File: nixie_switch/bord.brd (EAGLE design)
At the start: 20 x 25 mm, 2 parts, among them SW1 TVGP01-G73BB

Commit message: [fix] hole
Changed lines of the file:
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@@
 <wire x1="20" y1="25" x2="0" y2="25" width="0" layer="20"/>
 <wire x1="0" y1="25" x2="0" y2="0" width="0" layer="20"/>
-<hole x="2" y="23" drill="3.2"/>
-<hole x="18" y="23" drill="3.2"/>
-<hole x="18" y="2" drill="3.2"/>
-<hole x="2" y="2" drill="3.2"/>
+<hole x="17" y="6" drill="3.2"/>
+<hole x="3" y="6" drill="3.2"/>
 </plain>
 <attributes>

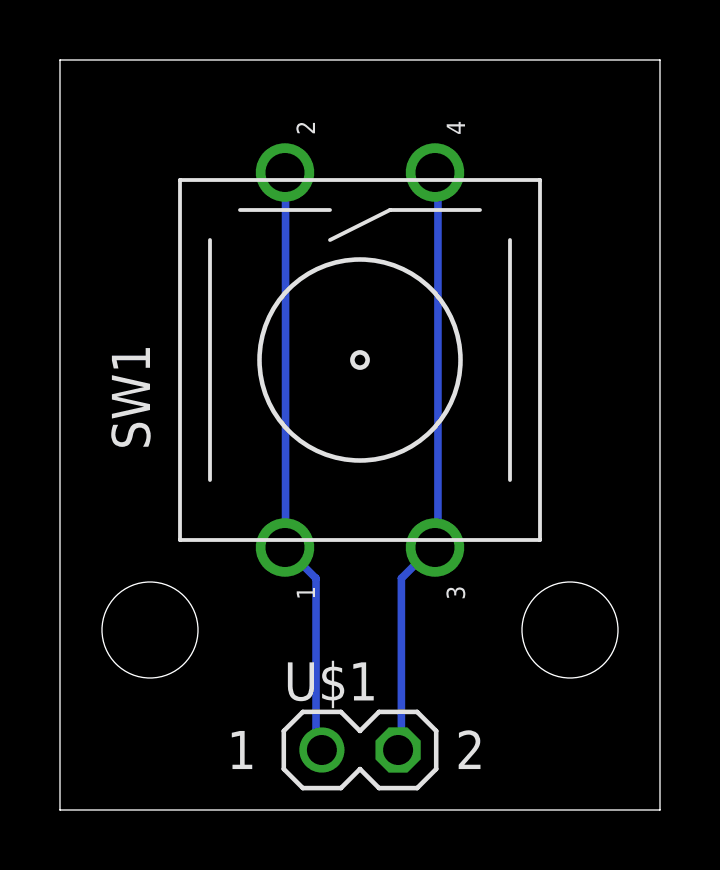
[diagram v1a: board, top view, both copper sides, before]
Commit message: [fix] 太さ・ガーバー出力(FusionPCB)
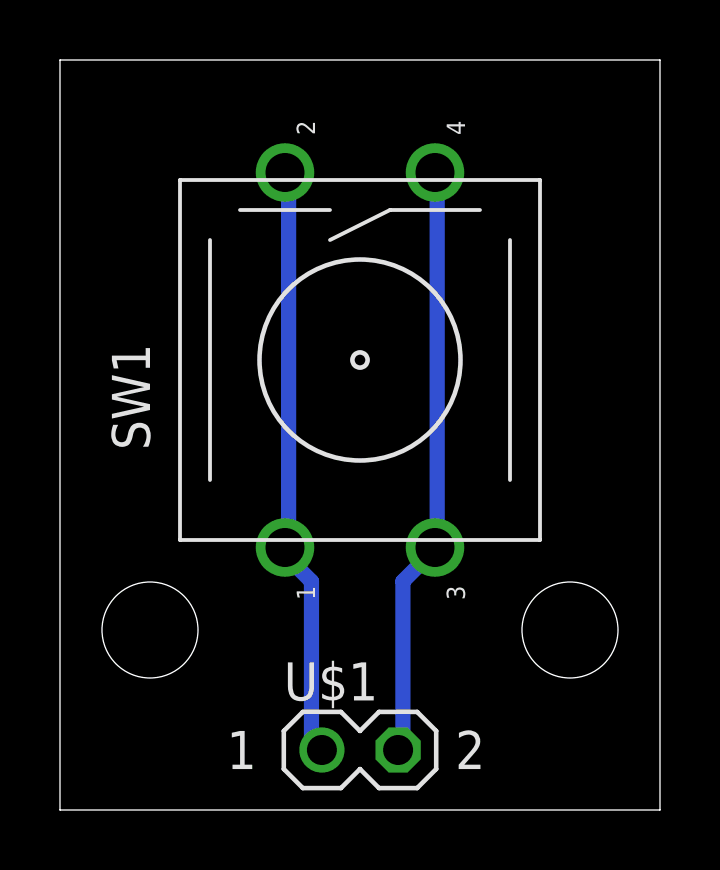
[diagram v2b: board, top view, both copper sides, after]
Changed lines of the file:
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@@
 <?xml version="1.0" encoding="utf-8"?>
 <!DOCTYPE eagle SYSTEM "eagle.dtd">
-<eagle version="8.6.0">
+<eagle version="8.5.2">
 <drawing>
 <settings>
@@
 </variantdefs>
 <classes>
-<class number="0" name="default" width="0.254" drill="0">
+<class number="0" name="default" width="0.508" drill="0">
+<clearance class="0" value="0.254"/>
 </class>
 </classes>
-<designrules name="default">
+<designrules name="SeeedStudio_2layer_DRU_no_angle_20140221">
 <description language="de">&lt;b&gt;EAGLE Design Rules&lt;/b&gt;
 &lt;p&gt;
@@
 necessary adjustments and save your customized
 design rules under a new name.</description>
+<description language="zh">&lt;b&gt;Seeed Studio EAGLE Design Rules&lt;/b&gt;
+</description>
 <param name="layerSetup" value="(1*16)"/>
-<param name="mtCopper" value="0.035mm 0.035mm 0.035mm 0.035mm 0.035mm 0.035mm 0.035mm 0.035mm 0.035mm 0.035mm 0.035mm 0.035mm 0.035mm 0.035mm 0.035mm 0.035mm"/>
-<param name="mtIsolate" value="1.5mm 0.15mm 0.2mm 0.15mm 0.2mm 0.15mm 0.2mm 0.15mm 0.2mm 0.15mm 0.2mm 0.15mm 0.2mm 0.15mm 0.2mm"/>
+<param name="mtCopper" value="0.035mm 0.0175mm 0.035mm 0.035mm 0.035mm 0.035mm 0.035mm 0.035mm 0.035mm 0.035mm 0.035mm 0.035mm 0.035mm 0.035mm 0.0175mm 0.035mm"/>
+<param name="mtIsolate" value="1.5mm 1.1mm 0.2mm 0.15mm 0.2mm 0.15mm 0.2mm 0.15mm 0.2mm 0.15mm 0.2mm 0.15mm 0.2mm 0.15mm 0.2mm"/>
 <param name="mdWireWire" value="6mil"/>
 <param name="mdWirePad" value="6mil"/>
@@
 <param name="mdPadVia" value="6mil"/>
 <param name="mdViaVia" value="6mil"/>
-<param name="mdSmdPad" value="6mil"/>
-<param name="mdSmdVia" value="6mil"/>
-<param name="mdSmdSmd" value="6mil"/>
-<param name="mdViaViaSameLayer" value="6mil"/>
+<param name="mdSmdPad" value="0mil"/>
+<param name="mdSmdVia" value="0mil"/>
+<param name="mdSmdSmd" value="0mil"/>
+<param name="mdViaViaSameLayer" value="8mil"/>
 <param name="mnLayersViaInSmd" value="2"/>
-<param name="mdCopperDimension" value="40mil"/>
-<param name="mdDrill" value="6mil"/>
+<param name="mdCopperDimension" value="10mil"/>
+<param name="mdDrill" value="10mil"/>
 <param name="mdSmdStop" value="0mil"/>
 <param name="msWidth" value="6mil"/>
-<param name="msDrill" value="0.35mm"/>
-<param name="msMicroVia" value="9.99mm"/>
+<param name="msDrill" value="12mil"/>
+<param name="msMicroVia" value="12mil"/>
 <param name="msBlindViaRatio" value="0.5"/>
 <param name="rvPadTop" value="0.25"/>
@@
 <param name="rlMinPadBottom" value="10mil"/>
 <param name="rlMaxPadBottom" value="20mil"/>
-<param name="rlMinViaOuter" value="8mil"/>
+<param name="rlMinViaOuter" value="6mil"/>
 <param name="rlMaxViaOuter" value="20mil"/>
-<param name="rlMinViaInner" value="8mil"/>
+<param name="rlMinViaInner" value="6mil"/>
 <param name="rlMaxViaInner" value="20mil"/>
 <param name="rlMinMicroViaOuter" value="4mil"/>
@@
 <param name="psTop" value="-1"/>
 <param name="psBottom" value="-1"/>
-<param name="psFirst" value="-1"/>
+<param name="psFirst" value="0"/>
 <param name="psElongationLong" value="100"/>
 <param name="psElongationOffset" value="100"/>
 <param name="mvStopFrame" value="1"/>
 <param name="mvCreamFrame" value="0"/>
-<param name="mlMinStopFrame" value="4mil"/>
-<param name="mlMaxStopFrame" value="4mil"/>
+<param name="mlMinStopFrame" value="2mil"/>
+<param name="mlMaxStopFrame" value="2mil"/>
 <param name="mlMinCreamFrame" value="0mil"/>
 <param name="mlMaxCreamFrame" value="0mil"/>
-<param name="mlViaStopLimit" value="0mil"/>
+<param name="mlViaStopLimit" value="100mil"/>
 <param name="srRoundness" value="0"/>
 <param name="srMinRoundness" value="0mil"/>
@@
 <param name="checkAngle" value="0"/>
 <param name="checkFont" value="1"/>
-<param name="checkRestrict" value="1"/>
+<param name="checkRestrict" value="0"/>
 <param name="checkStop" value="0"/>
 <param name="checkValues" value="0"/>
@@
 </autorouter>
 <elements>
-<element name="SW1" library="new" package="TVGP01-G73BB" value="TVGP01-G73BB" x="10" y="15" rot="R90"/>
-<element name="U$1" library="180118 Library by matsu" package="PIN_HEADER_MALE_1X02_02P" value="PIN_HEADER_MALE_1X02_02P" x="10" y="2"/>
+<element name="SW1" library="new" package="TVGP01-G73BB" value="TVGP01-G73BB" x="10" y="15" smashed="yes" rot="R90">
+<attribute name="NAME" x="3" y="12" size="1.27" layer="25" ratio="10" rot="R90"/>
+</element>
+<element name="U$1" library="180118 Library by matsu" package="PIN_HEADER_MALE_1X02_02P" value="PIN_HEADER_MALE_1X02_02P" x="10" y="2" smashed="yes">
+<attribute name="NAME" x="7.46" y="3.651" size="1.27" layer="25" ratio="10"/>
+</element>
 </elements>
 <signals>
@@
 <contactref element="SW1" pad="1"/>
 <contactref element="SW1" pad="2"/>
-<wire x1="8.5344" y1="7.7216" x2="8.5344" y2="2.032" width="0.254" layer="16"/>
-<wire x1="7.5184" y1="8.7376" x2="8.5344" y2="7.7216" width="0.254" layer="16"/>
-<wire x1="8.5344" y1="2.032" x2="8.73" y2="2" width="0.254" layer="16"/>
-<wire x1="7.5184" y1="8.7376" x2="7.5" y2="8.75" width="0.254" layer="16"/>
-<wire x1="7.5184" y1="8.9408" x2="7.5184" y2="21.1328" width="0.254" layer="16"/>
-<wire x1="7.5184" y1="21.1328" x2="7.5" y2="21.25" width="0.254" layer="16"/>
-<wire x1="7.5184" y1="8.9408" x2="7.5" y2="8.75" width="0.254" layer="16"/>
+<wire x1="8.382" y1="7.62" x2="8.382" y2="2.286" width="0.508" layer="16"/>
+<wire x1="7.62" y1="8.382" x2="8.382" y2="7.62" width="0.508" layer="16"/>
+<wire x1="8.382" y1="2.286" x2="8.73" y2="2" width="0.508" layer="16"/>
+<wire x1="7.62" y1="8.382" x2="7.5" y2="8.75" width="0.508" layer="16"/>
+<wire x1="7.62" y1="8.763" x2="7.62" y2="20.955" width="0.508" layer="16"/>
+<wire x1="7.62" y1="20.955" x2="7.5" y2="21.25" width="0.508" layer="16"/>
+<wire x1="7.62" y1="8.763" x2="7.5" y2="8.75" width="0.508" layer="16"/>
 </signal>
 <signal name="N$2">
@@
 <contactref element="SW1" pad="4"/>
 <contactref element="U$1" pad="P$2"/>
-<wire x1="11.3792" y1="7.7216" x2="11.3792" y2="2.032" width="0.254" layer="16"/>
-<wire x1="12.3952" y1="8.7376" x2="11.3792" y2="7.7216" width="0.254" layer="16"/>
-<wire x1="11.3792" y1="2.032" x2="11.27" y2="2" width="0.254" layer="16"/>
-<wire x1="12.3952" y1="8.7376" x2="12.5" y2="8.75" width="0.254" layer="16"/>
-<wire x1="12.5984" y1="8.9408" x2="12.5984" y2="21.1328" width="0.254" layer="16"/>
-<wire x1="12.5984" y1="21.1328" x2="12.5" y2="21.25" width="0.254" layer="16"/>
-<wire x1="12.5984" y1="8.9408" x2="12.5" y2="8.75" width="0.254" layer="16"/>
+<wire x1="11.43" y1="7.62" x2="11.43" y2="2.286" width="0.508" layer="16"/>
+<wire x1="12.192" y1="8.382" x2="11.43" y2="7.62" width="0.508" layer="16"/>
+<wire x1="11.43" y1="2.286" x2="11.27" y2="2" width="0.508" layer="16"/>
+<wire x1="12.192" y1="8.382" x2="12.5" y2="8.75" width="0.508" layer="16"/>
+<wire x1="12.573" y1="8.763" x2="12.573" y2="20.955" width="0.508" layer="16"/>
+<wire x1="12.573" y1="20.955" x2="12.5" y2="21.25" width="0.508" layer="16"/>
+<wire x1="12.573" y1="8.763" x2="12.5" y2="8.75" width="0.508" layer="16"/>
 </signal>
 </signals>
